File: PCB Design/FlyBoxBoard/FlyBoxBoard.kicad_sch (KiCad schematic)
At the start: 40 parts, among them J1 5V in, J10 RED, J11 GREEN, J12 WHITE, J13 INFRARED, J14 LCD Screen, J15 SD card reader, J16 5K Ohms, J17 5K Ohms, J18 ESP 32 Left Side extra pinouts, J19 ESP 32 Left Side extra pinouts, J2 12V in, J20 Transistor, J21 Logic Level LV pins, J22 Potentiometer, J23 Logic Level Left Side LV, J24 ESP 32 Right Side extra pinou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, J25 ESP 32 Right Side extra pinou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, J26 BuckPuck IR, J27 Logic Level Right Side HV, J28 Logic Level HV pins, J29 5K Ohms, J3 ESP 32 Left Side, J30 5K Ohms, J31 5K Ohms, J32 5K Ohms, J33 5K Ohms, J34 5K Ohms, J35 Transistor, J36 Transistor, J37 Transistor, J38 BuckPuck White, J39 BuckPuck Green, J4 Real Time Controller, J40 BuckPuck Red, J5 ESP 32 Right Side, J6 Extra pinouts 5V, J7 Extra pinouts 12V, J8 Extra pinouts GND, J9 FANS

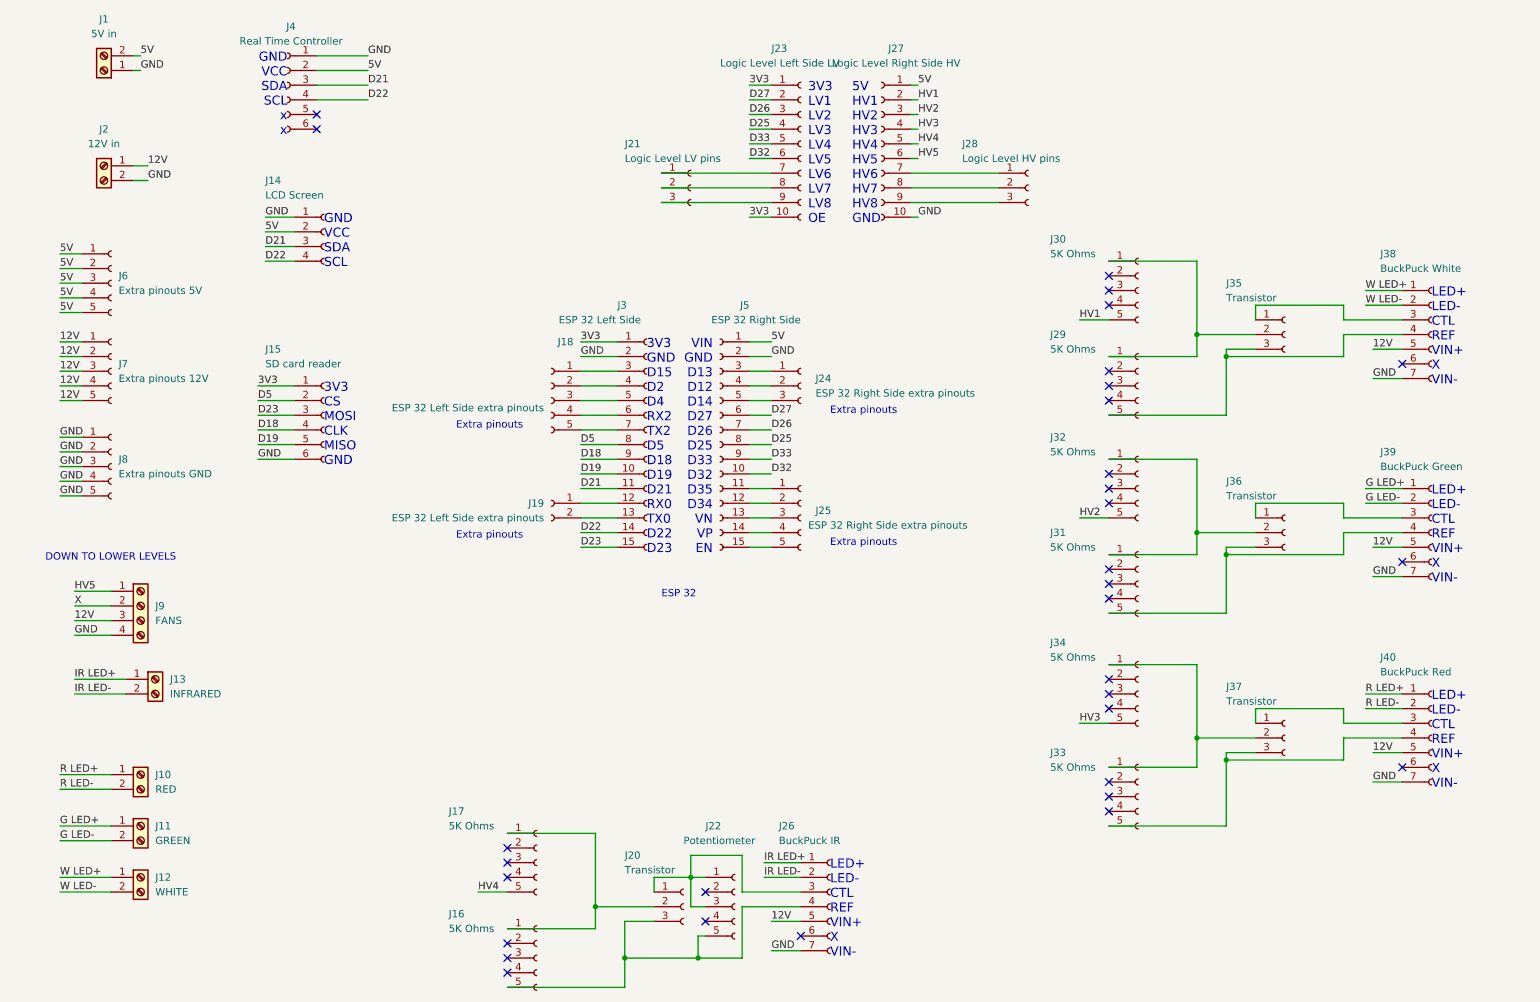
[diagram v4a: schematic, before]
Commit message: 3/8 Work
Missing button footprint
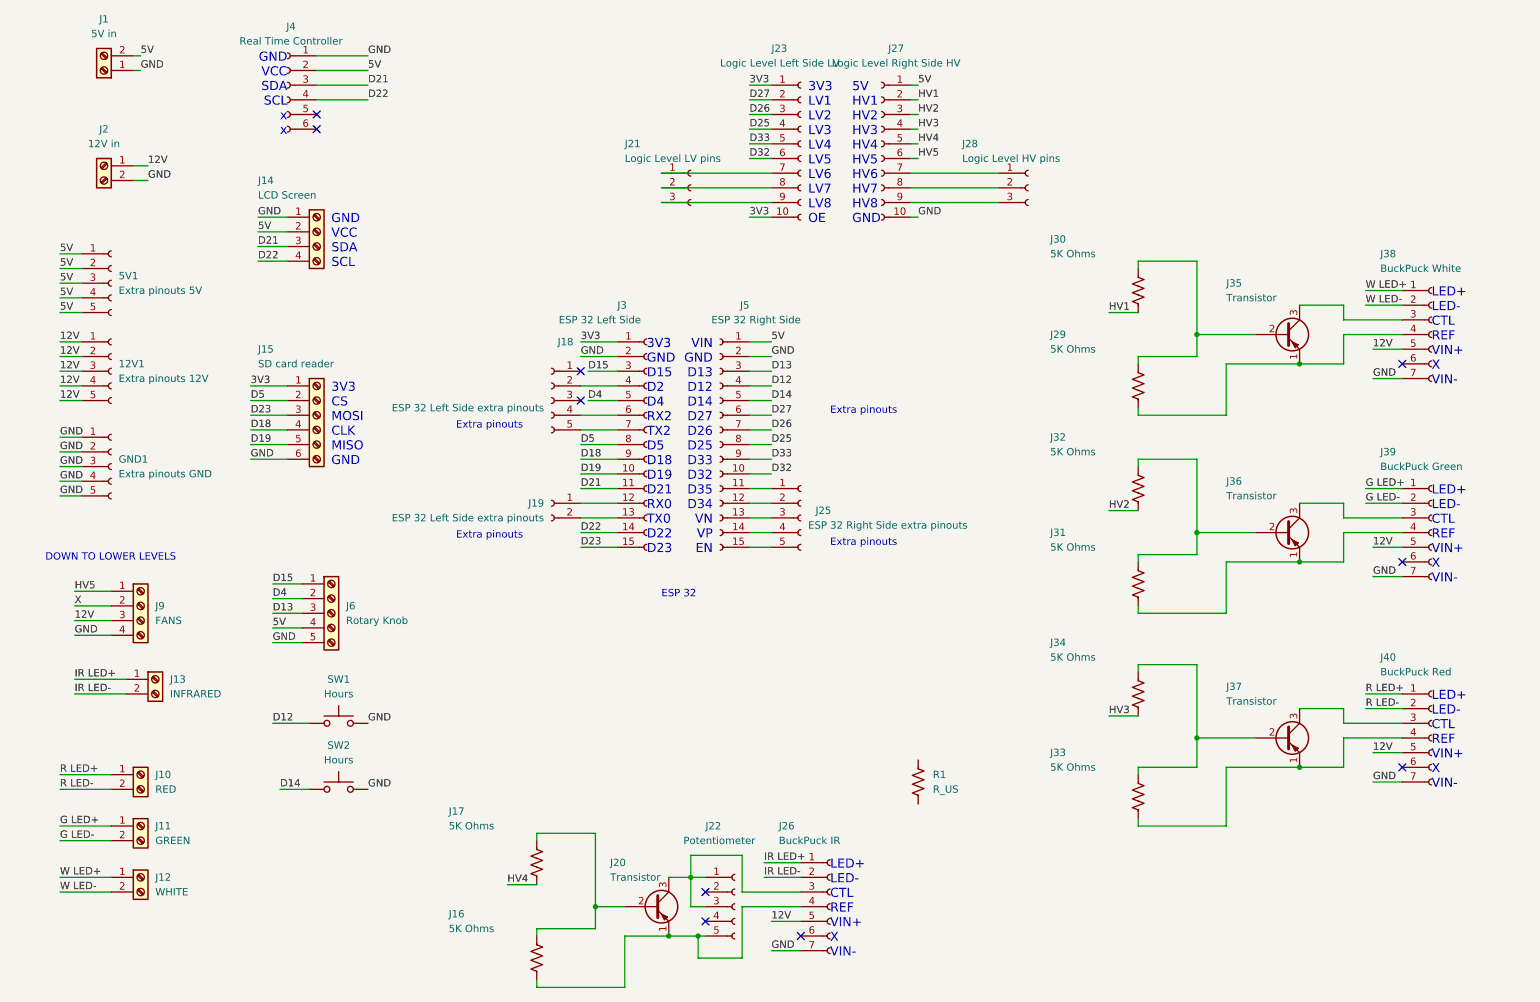
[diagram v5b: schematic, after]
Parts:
- removed J24: ESP 32 Right Side extra pinouts, Connector_PinSocket_2.54mm:PinSocket_1x03_P2.54mm_Vertical, symbol Connector:Conn_01x03_Female
- added J6: Rotary Knob, TerminalBlock:TerminalBlock_bornier-5_P5.08mm, symbol Connector:Screw_Terminal_01x05
- added R1: R_US, Resistor_SMD:R_0805_2012Metric_Pad1.20x1.40mm_HandSolder, symbol Device:R_US
- added SW1, SW2: Hours, symbol Switch:SW_Push
- J14: footprint Connector_PinSocket_2.54mm:PinSocket_1x04_P2.54mm_Vertical -> TerminalBlock:TerminalBlock_bornier-4_P5.08mm; symbol Connector:Conn_01x04_Female -> Connector:Screw_Terminal_01x04
- J15: footprint Connector_PinSocket_2.54mm:PinSocket_1x06_P2.54mm_Vertical -> TerminalBlock:TerminalBlock_bornier-6_P5.08mm; symbol Connector:Conn_01x06_Female -> Connector:Screw_Terminal_01x06
- J16, J17, J29, J30, J31, J32, J33, J34: footprint Connector_PinSocket_2.54mm:PinSocket_1x05_P2.54mm_Vertical -> Resistor_SMD:R_0805_2012Metric_Pad1.20x1.40mm_HandSolder; symbol Connector:Conn_01x05_Female -> Device:R_US
- J20, J35, J36, J37: footprint Connector_PinSocket_2.54mm:PinSocket_1x03_P2.54mm_Vertical -> Package_TO_SOT_THT:TO-92_Inline; symbol Connector:Conn_01x03_Female -> Transistor_BJT:2N3906
- J9: footprint Connector_PinSocket_2.54mm:PinSocket_1x04_P2.54mm_Vertical -> TerminalBlock:TerminalBlock_bornier-4_P5.08mm
- renumbered J7 to 12V1, J6 to 5V1, J8 to GND1
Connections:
- net 5V: now also J6.4 (Pin_4)
- net GND: now also J6.5 (Pin_5), SW1.2, SW2.2
- net HV1: now also J30.2; no longer J30.5 (Pin_5)
- net HV2: now also J32.2; no longer J32.5 (Pin_5)
- net HV3: now also J34.2; no longer J34.5 (Pin_5)
- net HV4: now also J17.2; no longer J17.5 (Pin_5)
- net at J22.1 (Pin_1), J22.3 (Pin_3), J26.3 (Pin_3): now also J20.3 (C); no longer J20.1 (Pin_1)
- net at J22.5 (Pin_5), J26.4 (Pin_4): now also J16.2, J20.1 (E); no longer J16.5 (Pin_5), J20.3 (Pin_3)
- net at J35.1 (E): now also J29.2, J38.4 (Pin_4); no longer J38.3 (Pin_3)
- net at J40.3 (Pin_3): now also J37.3 (C); no longer J37.1 (Pin_1)
- net at J31.2: now also J36.1 (E), J39.4 (Pin_4)
- net at J39.3 (Pin_3): now also J36.3 (C); no longer J36.1 (Pin_1)
- net at J18.1 (Pin_1): no longer J3.3 (Pin_3)
- net at J18.3 (Pin_3): no longer J3.5 (Pin_5)
- net at J33.2: now also J37.1 (E), J40.4 (Pin_4)
- net D13: now reaches J5.3 (Pin_3)
- net D13: now also J6.3 (Pin_3)
- net D12: now reaches J5.4 (Pin_4)
- net D12: now also SW1.1
- net D14: now reaches J5.5 (Pin_5)
- net D14: now also SW2.1
- new net: J35.3 (C), J38.3 (Pin_3)
- new net D15: J3.3 (Pin_3), J6.1 (Pin_1)
- new net D4: J3.5 (Pin_5), J6.2 (Pin_2)
- no-connect marks 32 -> 10
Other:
- moved on the sheet: J20, J35, J36, J37

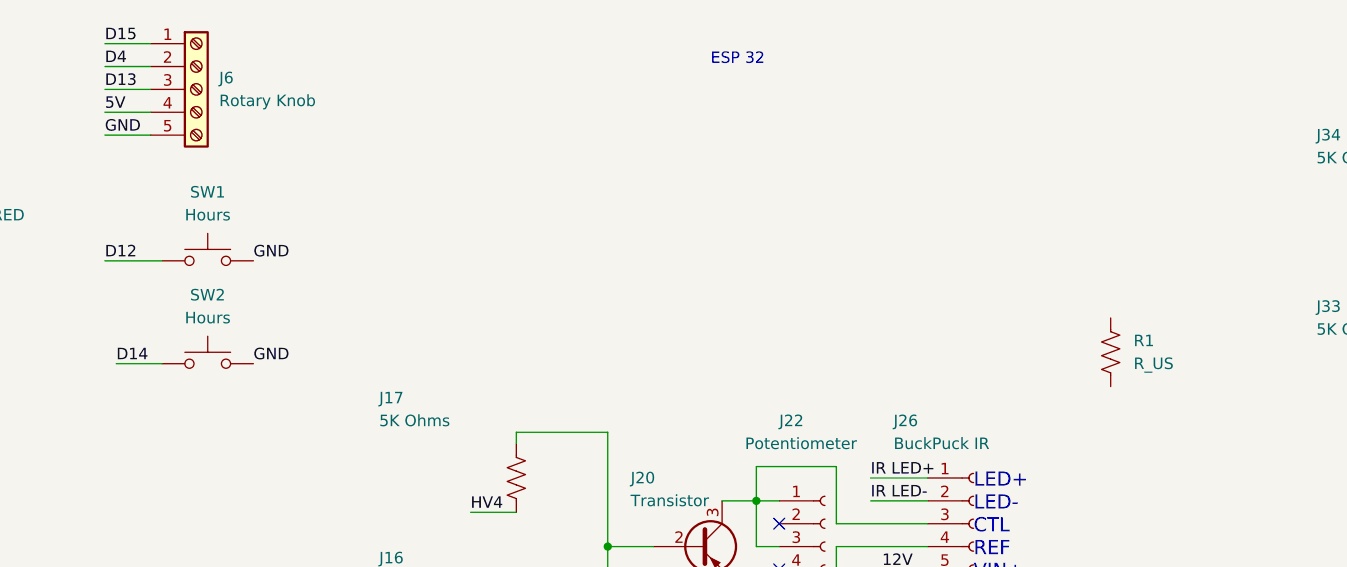
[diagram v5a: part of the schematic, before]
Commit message: V2 IR and RGW boards done
Main board missing button footprint
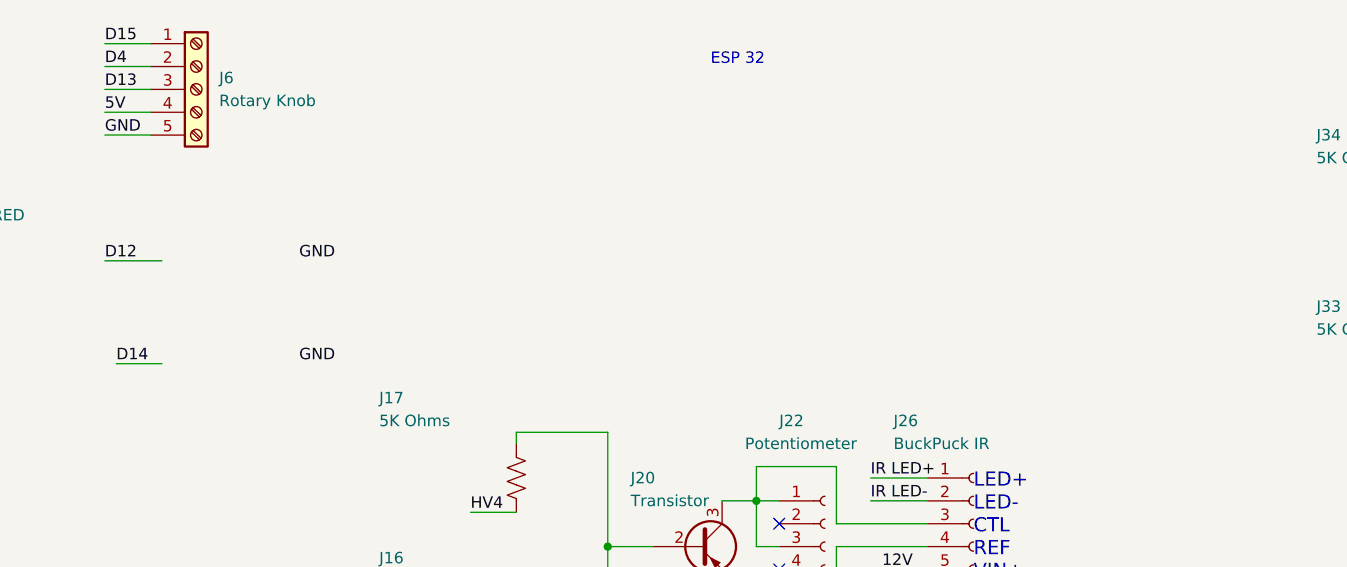
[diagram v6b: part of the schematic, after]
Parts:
- removed R1: R_US, Resistor_SMD:R_0805_2012Metric_Pad1.20x1.40mm_HandSolder, symbol Device:R_US
- removed SW1, SW2: Hours, symbol Switch:SW_Push
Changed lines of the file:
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@@
     (effects (font (size 1.27 1.27)) (justify left bottom))
   )
-  (label "GND" (at 71.12 152.4 0)
+  (label "GND" (at 76.2 152.4 0)
     (effects (font (size 1.27 1.27)) (justify left bottom))
   )
@@
     (effects (font (size 1.27 1.27)) (justify left bottom))
   )
-  (label "GND" (at 71.12 140.97 0)
+  (label "GND" (at 76.2 140.97 0)
     (effects (font (size 1.27 1.27)) (justify left bottom))
   )
@@
     (pin "4")
     (pin "5")
-  )
-  (symbol (lib_id "Switch:SW_Push") (at 66.04 140.97 0) (unit 1)
-    (in_bom yes) (on_board yes) (fields_autoplaced)
-    (property "Reference" "SW1" (id 0) (at 66.04 133.35 0))
-    (property "Value" "Hours" (id 1) (at 66.04 135.89 0))
-    (property "Footprint" "" (id 2) (at 66.04 135.89 0)
-      (effects (font (size 1.27 1.27)) hide)
-    )
-    (property "Datasheet" "~" (id 3) (at 66.04 135.89 0)
-      (effects (font (size 1.27 1.27)) hide)
-    )
-    (pin "1")
-    (pin "2")
   )
   (symbol (lib_id "Connector:Conn_01x10_Female") (at 146.05 40.64 0) (unit 1)
@@
     (pin "9")
   )
-  (symbol (lib_id "Device:R_US") (at 166.37 151.13 0) (unit 1)
-    (in_bom yes) (on_board yes) (fields_autoplaced)
-    (property "Reference" "R1" (id 0) (at 168.91 149.8599 0)
-      (effects (font (size 1.27 1.27)) (justify left))
-    )
-    (property "Value" "R_US" (id 1) (at 168.91 152.3999 0)
-      (effects (font (size 1.27 1.27)) (justify left))
-    )
-    (property "Footprint" "Resistor_SMD:R_0805_2012Metric_Pad1.20x1.40mm_HandSolder" (id 2) (at 167.386 151.384 90)
-      (effects (font (size 1.27 1.27)) hide)
-    )
-    (property "Datasheet" "~" (id 3) (at 166.37 151.13 0)
-      (effects (font (size 1.27 1.27)) hide)
-    )
-    (pin "1")
-    (pin "2")
-  )
   (symbol (lib_id "Connector:Screw_Terminal_01x04") (at 31.75 120.65 0) (unit 1)
     (in_bom yes) (on_board yes) (fields_autoplaced)
@@
     )
     (property "Datasheet" "~" (id 3) (at 100.33 165.1 0)
-      (effects (font (size 1.27 1.27)) hide)
-    )
-    (pin "1")
-    (pin "2")
-  )
-  (symbol (lib_id "Switch:SW_Push") (at 66.04 152.4 0) (unit 1)
-    (in_bom yes) (on_board yes) (fields_autoplaced)
-    (property "Reference" "SW2" (id 0) (at 66.04 144.78 0))
-    (property "Value" "Hours" (id 1) (at 66.04 147.32 0))
-    (property "Footprint" "" (id 2) (at 66.04 147.32 0)
-      (effects (font (size 1.27 1.27)) hide)
-    )
-    (property "Datasheet" "~" (id 3) (at 66.04 147.32 0)
       (effects (font (size 1.27 1.27)) hide)
     )
@@
       (reference "J40") (unit 1) (value "BuckPuck Red") (footprint "Connector_PinSocket_2.54mm:PinSocket_1x07_P2.54mm_Vertical")
     )
-    (path "/b772f476-b7d4-4c3b-b651-02777418ee51"
-      (reference "R1") (unit 1) (value "R_US") (footprint "Resistor_SMD:R_0805_2012Metric_Pad1.20x1.40mm_HandSolder")
-    )
-    (path "/8c3a813e-1e2d-4f34-80d4-a0a76e5afed7"
-      (reference "SW1") (unit 1) (value "Hours") (footprint "")
-    )
-    (path "/d93e2a7b-4062-40a2-bc24-19b6e849eca7"
-      (reference "SW2") (unit 1) (value "Hours") (footprint "")
-    )
-  )
+  )

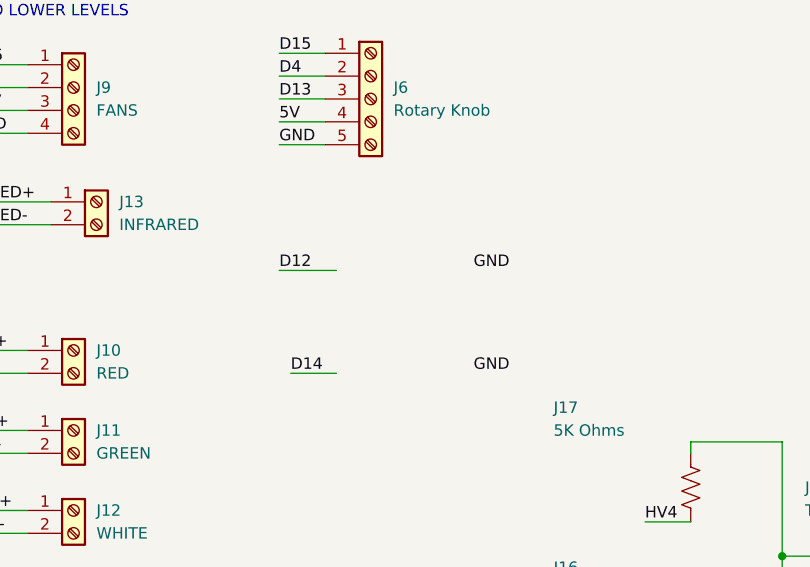
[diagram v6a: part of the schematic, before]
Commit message: Finished V2 PCBs with rounded edges
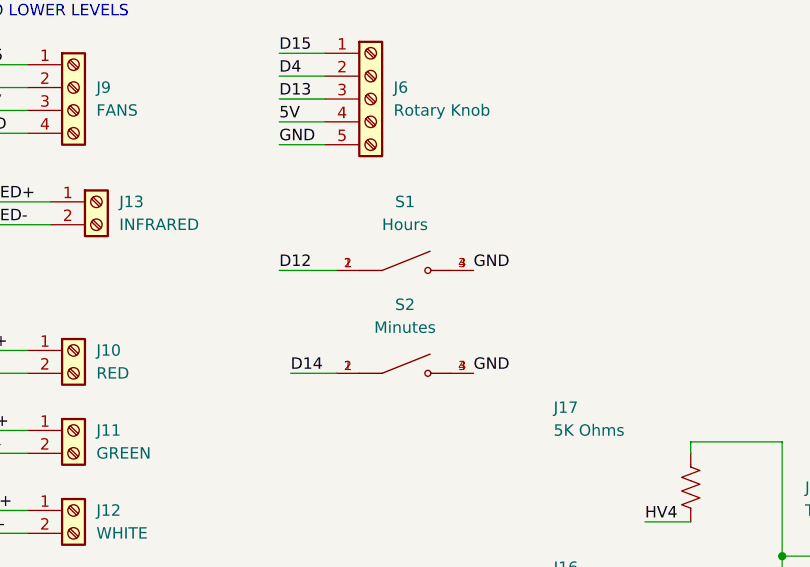
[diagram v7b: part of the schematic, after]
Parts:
- added S1: Hours, SW_1571563-2, symbol SnapEDA-Library:1571563-2
- added S2: Minutes, SW_1571563-2, symbol SnapEDA-Library:1571563-2
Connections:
- net D12: now also S1.1, S1.2
- net D14: now also S2.1, S2.2
- net GND: now also S1.3, S1.4, S2.3, S2.4
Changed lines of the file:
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@@
     (pin "5")
+  )
+  (symbol (lib_id "SnapEDA-Library:1571563-2") (at 68.58 140.97 0) (unit 1)
+    (in_bom yes) (on_board yes) (fields_autoplaced)
+    (property "Reference" "S1" (id 0) (at 68.58 133.35 0))
+    (property "Value" "Hours" (id 1) (at 68.58 135.89 0))
+    (property "Footprint" "SW_1571563-2" (id 2) (at 68.58 140.97 0)
+      (effects (font (size 1.27 1.27)) (justify left bottom) hide)
+    )
+    (property "Datasheet" "" (id 3) (at 68.58 140.97 0)
+      (effects (font (size 1.27 1.27)) (justify left bottom) hide)
+    )
+    (property "MAXIMUM_PACKAGE_HEIGHT" "6.73mm" (id 4) (at 68.58 140.97 0)
+      (effects (font (size 1.27 1.27)) (justify left bottom) hide)
+    )
+    (property "STANDARD" "Manufacturer Recommendations" (id 5) (at 68.58 140.97 0)
+      (effects (font (size 1.27 1.27)) (justify left bottom) hide)
+    )
+    (property "PARTREV" "V" (id 6) (at 68.58 140.97 0)
+      (effects (font (size 1.27 1.27)) (justify left bottom) hide)
+    )
+    (property "MANUFACTURER" "TE" (id 7) (at 68.58 140.97 0)
+      (effects (font (size 1.27 1.27)) (justify left bottom) hide)
+    )
+    (pin "1")
+    (pin "2")
+    (pin "3")
+    (pin "4")
+  )
+  (symbol (lib_id "SnapEDA-Library:1571563-2") (at 68.58 152.4 0) (unit 1)
+    (in_bom yes) (on_board yes) (fields_autoplaced)
+    (property "Reference" "S2" (id 0) (at 68.58 144.78 0))
+    (property "Value" "Minutes" (id 1) (at 68.58 147.32 0))
+    (property "Footprint" "SW_1571563-2" (id 2) (at 68.58 152.4 0)
+      (effects (font (size 1.27 1.27)) (justify left bottom) hide)
+    )
+    (property "Datasheet" "" (id 3) (at 68.58 152.4 0)
+      (effects (font (size 1.27 1.27)) (justify left bottom) hide)
+    )
+    (property "MAXIMUM_PACKAGE_HEIGHT" "6.73mm" (id 4) (at 68.58 152.4 0)
+      (effects (font (size 1.27 1.27)) (justify left bottom) hide)
+    )
+    (property "STANDARD" "Manufacturer Recommendations" (id 5) (at 68.58 152.4 0)
+      (effects (font (size 1.27 1.27)) (justify left bottom) hide)
+    )
+    (property "PARTREV" "V" (id 6) (at 68.58 152.4 0)
+      (effects (font (size 1.27 1.27)) (justify left bottom) hide)
+    )
+    (property "MANUFACTURER" "TE" (id 7) (at 68.58 152.4 0)
+      (effects (font (size 1.27 1.27)) (justify left bottom) hide)
+    )
+    (pin "1")
+    (pin "2")
+    (pin "3")
+    (pin "4")
   )
   (symbol (lib_id "Connector:Screw_Terminal_01x02") (at 25.4 44.45 0) (mirror y) (unit 1)
@@
       (reference "J40") (unit 1) (value "BuckPuck Red") (footprint "Connector_PinSocket_2.54mm:PinSocket_1x07_P2.54mm_Vertical")
     )
-  )
+    (path "/65566512-aff2-40f3-b034-bdf3badc2e74"
+      (reference "S1") (unit 1) (value "Hours") (footprint "SW_1571563-2")
+    )
+    (path "/6a900db2-4eca-4b5e-8a29-46f9f2b1c6f0"
+      (reference "S2") (unit 1) (value "Minutes") (footprint "SW_1571563-2")
+    )
+  )
